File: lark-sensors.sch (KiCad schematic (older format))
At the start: 10 parts, among them IC1 MS5611-01BA03, IC2 MS5611-01BA03, U8 BMX055, U9 MS5525DSO

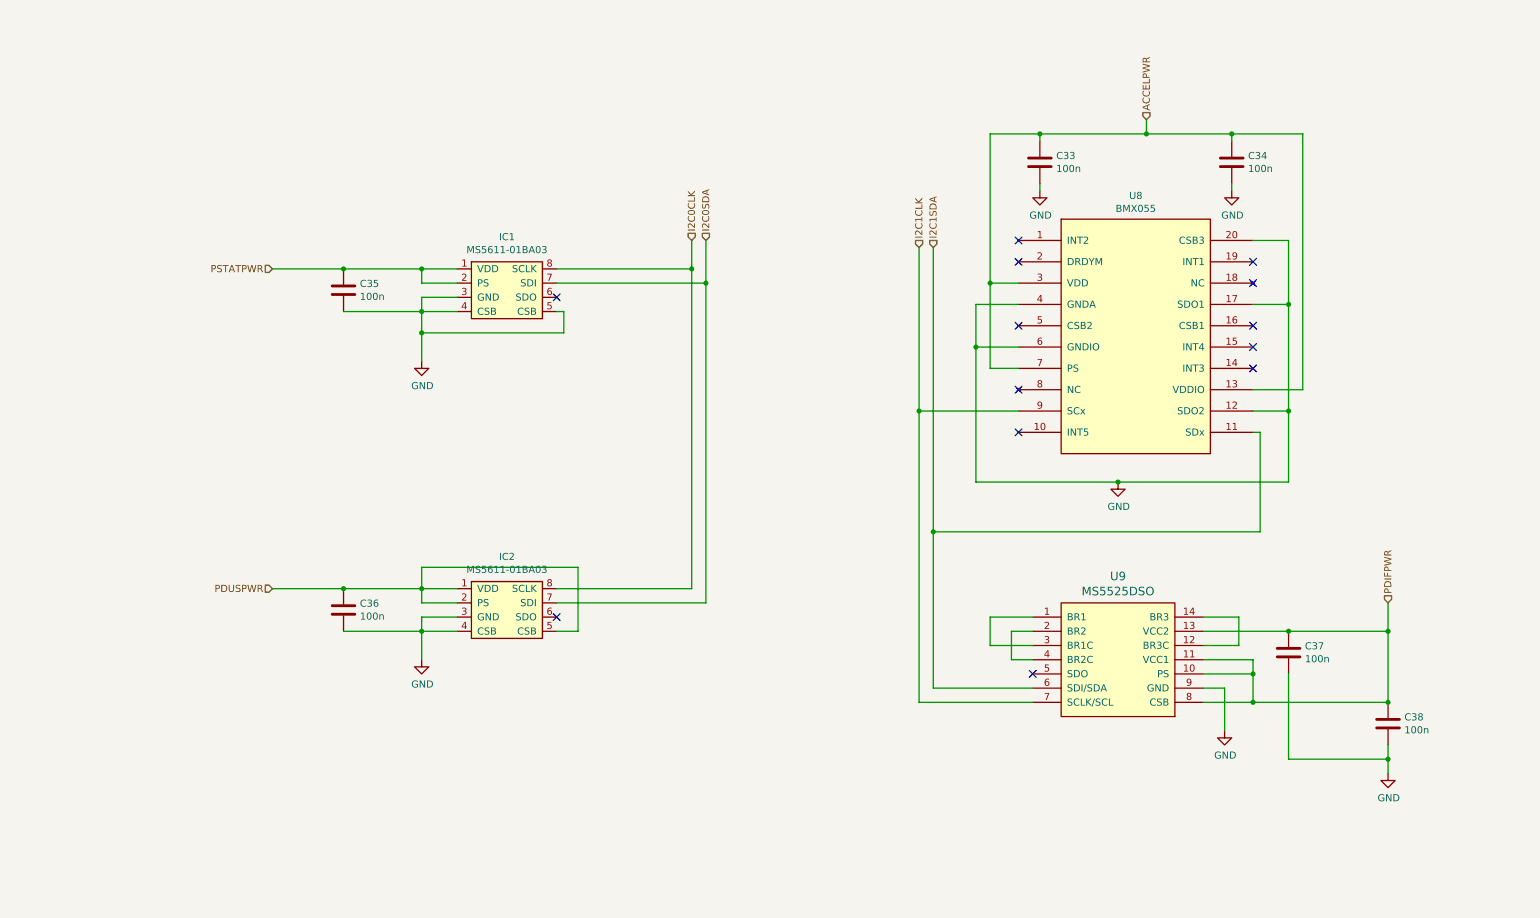
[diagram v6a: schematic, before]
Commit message: Updating schematic for the first prototype
* U1 can supply up to 600 mA
* drop USB charger for now
* smaller type of DC/DC (U2) for input
* remove one of the large capacitors
* change BMX interface to 4-wire SPI for speed reasons
* add I2C mux for pressure sensors

The changes were made during the meeting with Tomas.

BMX055 will be replaced by BMX088. For mechanical reasons, the pressure
sensors will be placed on a daughterboard. The daughterboard could get
footprints for different kinds pressure sensors (i.e. BMP388, HCLA0025).
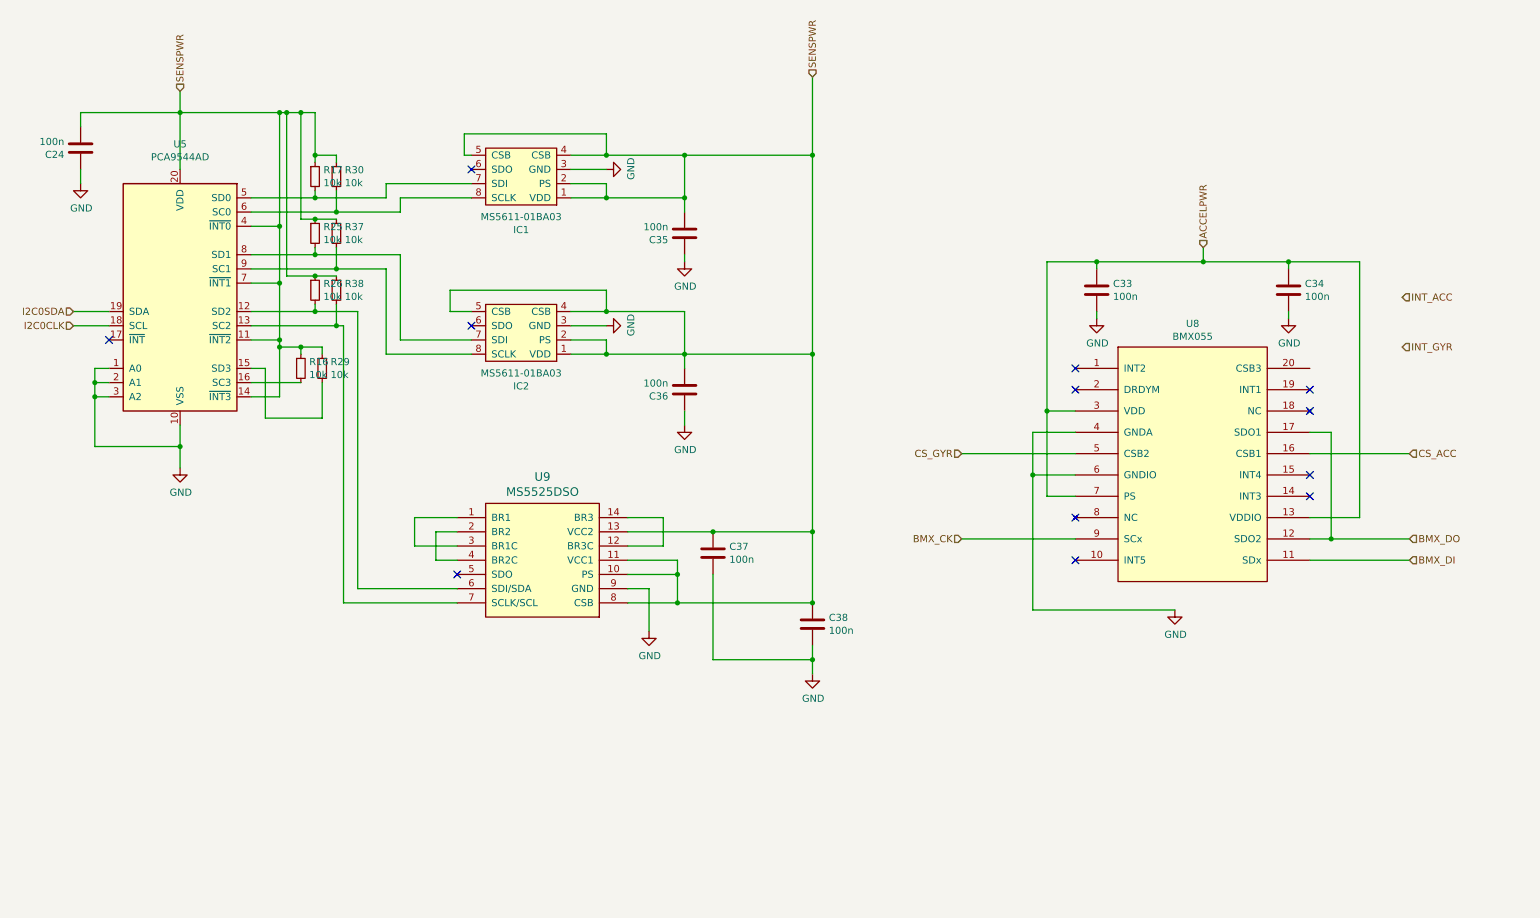
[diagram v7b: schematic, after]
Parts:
- added C24: 100n, Capacitor_SMD:C_0805_2012Metric_Pad1.15x1.40mm_HandSolder, symbol lark-rescue:C-Device
- added R16, R17, R25, R26, R29, R30, R37, R38: 10k, Resistor_SMD:R_0805_2012Metric_Pad1.15x1.40mm_HandSolder, symbol Device:R_Small
- added U5: PCA9544AD, Package_SO:SOIC-20W_7.5x12.8mm_P1.27mm, symbol Interface_Expansion:PCA9544AD
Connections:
- net GND: now also C35.1, C36.1, C24.1, U5.1 (A0), U5.10 (VSS), U5.2 (A1), U5.3 (A2); no longer C35.2, C36.2, IC1.4 (CSB), IC1.5 (CSB), IC2.4 (CSB), U8.12 (SDO2), U8.17 (SDO1), U8.20 (CSB3)
- net I2C0CLK: now also U5.18 (SCL); no longer IC1.8 (SCLK), IC2.8 (SCLK)
- net I2C0SDA: now also U5.19 (SDA); no longer IC1.7 (SDI), IC2.7 (SDI)
- net CS_ACC: now reaches U8.16 (CSB1)
- net CS_GYR: now reaches U8.5 (CSB2)
- net I2C1CLK: no longer names the net of U9.7 (SCLK/SCL)
- net I2C1CLK: now also R38.2, U5.13 (SC2); no longer U8.9 (SCx)
- net I2C1SDA: no longer names the net of U9.6 (SDI/SDA)
- net I2C1SDA: now also R26.2, U5.12 (SD2); no longer U8.11 (SDx)
- net PDIFPWR renamed SENSPWR
- net SENSPWR: now also C35.2, C36.2, IC1.1 (VDD), IC1.2 (PS), IC1.4 (CSB), IC1.5 (CSB), IC2.1 (VDD), IC2.2 (PS), IC2.4 (CSB), IC2.5 (CSB), C24.2, R16.1, R17.1, R25.1, R26.1, R29.1, R30.1, R37.1, R38.1, U5.11 (~INT2), U5.14 (~INT3), U5.20 (VDD), U5.4 (~INT0), U5.7 (~INT1)
- removed net PDUSPWR: C36.1, IC2.1 (VDD), IC2.2 (PS), IC2.5 (CSB)
- removed net PSTATPWR: C35.1, IC1.1 (VDD), IC1.2 (PS)
- new net: IC1.7 (SDI), R17.2, U5.5 (SD0)
- new net: IC1.8 (SCLK), R30.2, U5.6 (SC0)
- new net: IC2.7 (SDI), R25.2, U5.8 (SD1)
- new net: IC2.8 (SCLK), R37.2, U5.9 (SC1)
- new net: R29.2, U5.15 (SD3)
- new net: R16.2, U5.16 (SC3)
- new net BMX_CK: U8.9 (SCx)
- new net BMX_DI: U8.11 (SDx)
- new net BMX_DO: U8.12 (SDO2), U8.17 (SDO1)
- no-connect marks 13 -> 12
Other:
- moved on the sheet: C33, C34, C35, C36, C37, C38, IC1, IC2, U8, U9

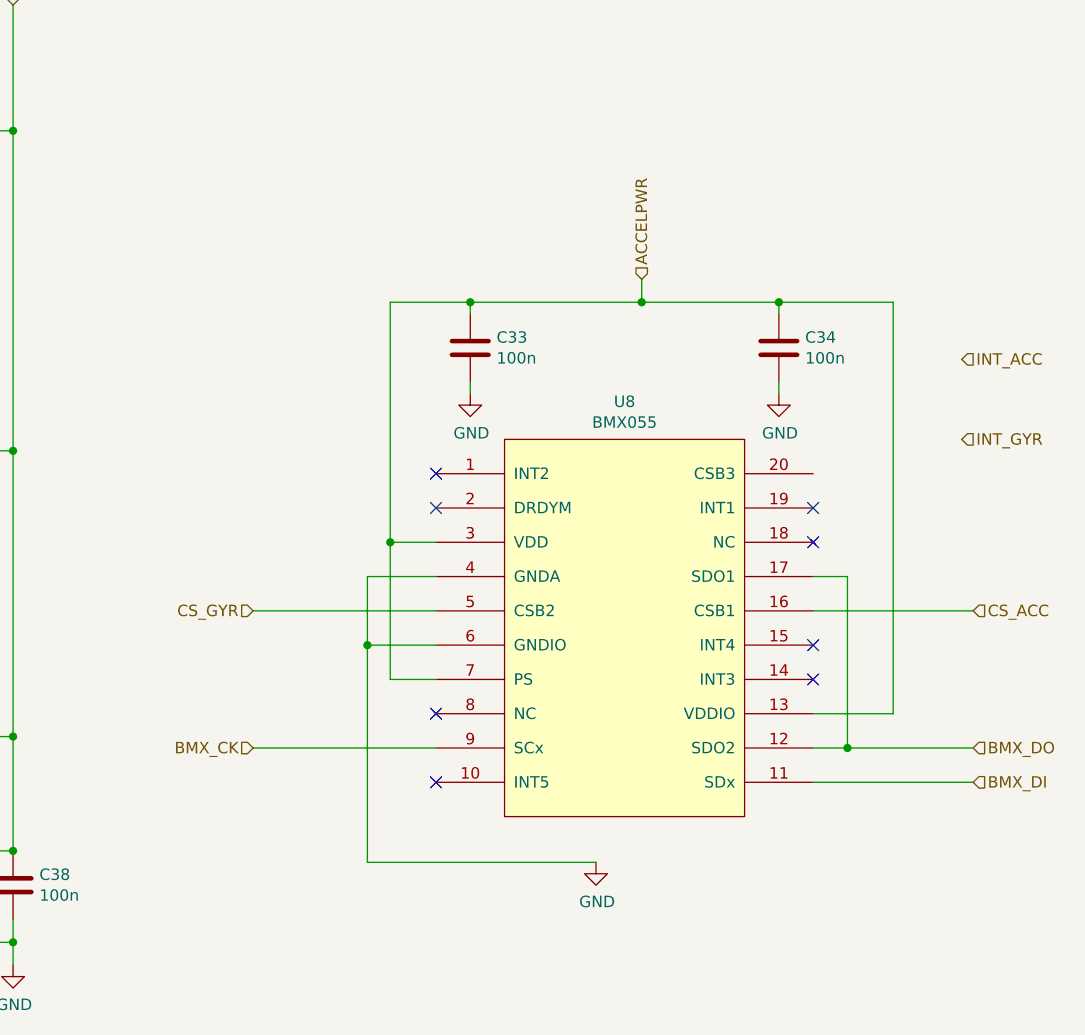
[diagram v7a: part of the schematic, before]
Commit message: Use BMI088 instead of BMX055.
Symbol for BMI088 was created and placed in the schematic.

Still looking for a LGA-16 4.5x3.0 footprint. Do we really need to
create that ourselves?
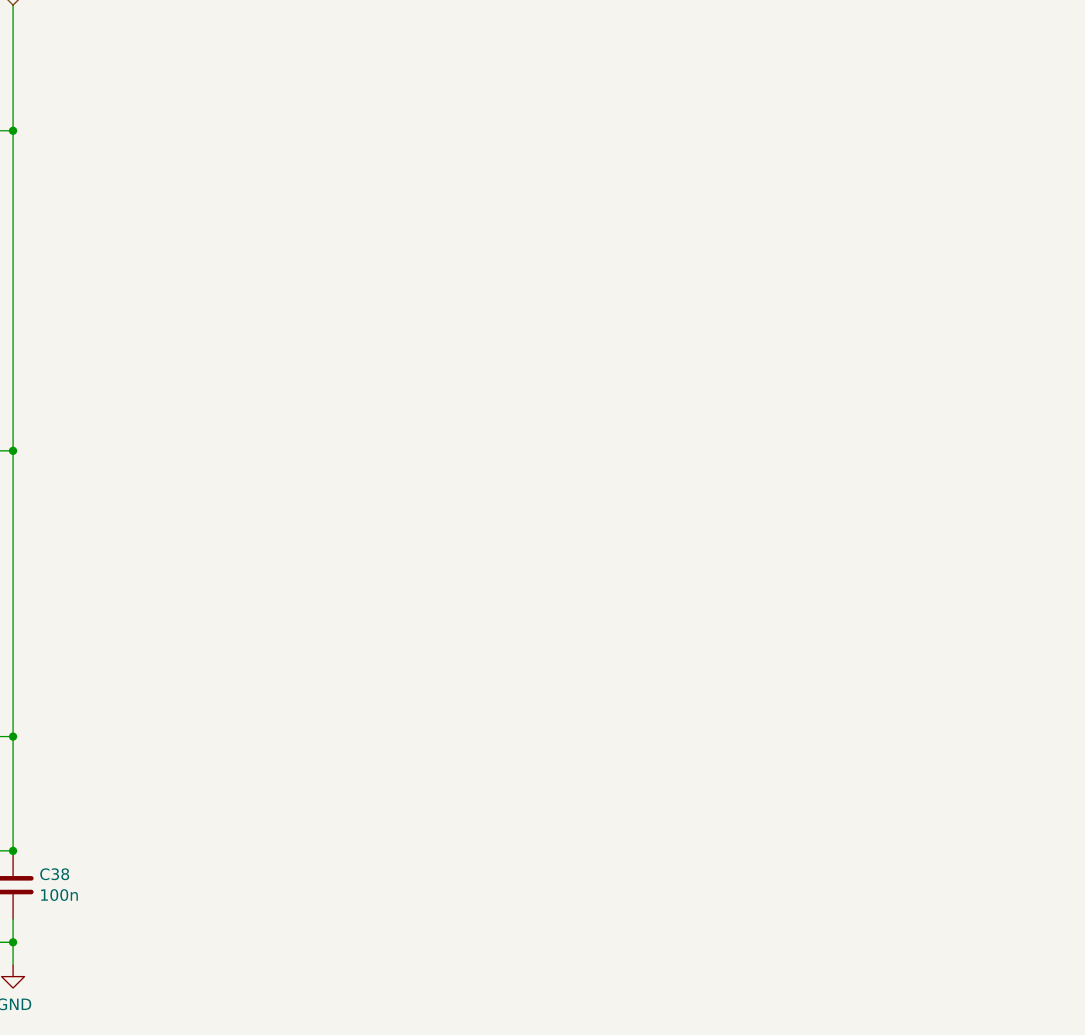
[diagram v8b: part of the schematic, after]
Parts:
- removed C33, C34: 100n, Capacitor_SMD:C_0805_2012Metric_Pad1.15x1.40mm_HandSolder, symbol lark-rescue:C-Device
- removed U8: BMX055, BMX055:BMX055, symbol lark-rescue:BMX055-bmx055
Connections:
- no-connect marks 12 -> 4
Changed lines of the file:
@@
 Text HLabel 1050 2650 0    50   Input ~ 0
 I2C0SDA
-$Comp
-L lark-rescue:GND-power #PWR038
-U 1 1 5C58F414
-P 8800 4750
-F 0 "#PWR038" H 8800 4500 50  0001 C CNN
-F 1 "GND" H 8805 4577 50  0000 C CNN
-F 2 "" H 8800 4750 50  0001 C CNN
-F 3 "" H 8800 4750 50  0001 C CNN
-	1    8800 4750
-	1    0    0    -1
-$EndComp
-$Comp
-L lark-rescue:C-Device C34
-U 1 1 5C593811
-P 9600 2500
-F 0 "C34" H 9715 2546 50  0000 L CNN
-F 1 "100n" H 9715 2455 50  0000 L CNN
-F 2 "Capacitor_SMD:C_0805_2012Metric_Pad1.15x1.40mm_HandSolder" H 9638 2350 50  0001 C CNN
-F 3 "~" H 9600 2500 50  0001 C CNN
-F 4 "885012207128" H 9600 2500 50  0001 C CNN "MPN"
-	1    9600 2500
-	1    0    0    -1
-$EndComp
-$Comp
-L lark-rescue:C-Device C33
-U 1 1 5C593886
-P 8250 2500
-F 0 "C33" H 8365 2546 50  0000 L CNN
-F 1 "100n" H 8365 2455 50  0000 L CNN
-F 2 "Capacitor_SMD:C_0805_2012Metric_Pad1.15x1.40mm_HandSolder" H 8288 2350 50  0001 C CNN
-F 3 "~" H 8250 2500 50  0001 C CNN
-F 4 "885012207128" H 8250 2500 50  0001 C CNN "MPN"
-	1    8250 2500
-	1    0    0    -1
-$EndComp
-Text HLabel 9000 2200 1    50   Input ~ 0
-ACCELPWR
-$Comp
-L lark-rescue:GND-power #PWR036
-U 1 1 5C59D0F5
-P 9600 2700
-F 0 "#PWR036" H 9600 2450 50  0001 C CNN
-F 1 "GND" H 9605 2527 50  0000 C CNN
-F 2 "" H 9600 2700 50  0001 C CNN
-F 3 "" H 9600 2700 50  0001 C CNN
-	1    9600 2700
-	1    0    0    -1
-$EndComp
-$Comp
-L lark-rescue:GND-power #PWR035
-U 1 1 5C59D1AD
-P 8250 2700
-F 0 "#PWR035" H 8250 2450 50  0001 C CNN
-F 1 "GND" H 8255 2527 50  0000 C CNN
-F 2 "" H 8250 2700 50  0001 C CNN
-F 3 "" H 8250 2700 50  0001 C CNN
-	1    8250 2700
-	1    0    0    -1
-$EndComp
 Wire Wire Line
 	5550 4200 6250 4200
@@
 	4800 1850 5350 1850
 NoConn ~ 3850 1650
-NoConn ~ 9750 3350
-NoConn ~ 9750 3200
-NoConn ~ 8100 4100
-NoConn ~ 8100 4400
-Wire Wire Line
-	9750 4100 10100 4100
-Wire Wire Line
-	10100 4100 10100 2300
-Wire Wire Line
-	8100 3350 7900 3350
-Wire Wire Line
-	7900 3350 7900 2300
-NoConn ~ 9750 3800
-NoConn ~ 9750 3950
-NoConn ~ 8100 3050
-NoConn ~ 8100 3200
-Wire Wire Line
-	7900 3350 7900 3950
-Wire Wire Line
-	7900 3950 8100 3950
-Connection ~ 7900 3350
-Wire Wire Line
-	8100 3500 7800 3500
-Wire Wire Line
-	7800 4750 8800 4750
-Wire Wire Line
-	8100 3800 7800 3800
-Wire Wire Line
-	7900 2300 8250 2300
-Wire Wire Line
-	8250 2350 8250 2300
-Connection ~ 8250 2300
-Wire Wire Line
-	8250 2700 8250 2650
-Wire Wire Line
-	9600 2350 9600 2300
-Connection ~ 9600 2300
-Wire Wire Line
-	9600 2300 10100 2300
-Wire Wire Line
-	9600 2650 9600 2700
-Wire Wire Line
-	8250 2300 9000 2300
-Wire Wire Line
-	9000 2200 9000 2300
-Connection ~ 9000 2300
-Wire Wire Line
-	9000 2300 9600 2300
 Wire Wire Line
 	3850 1850 3350 1850
@@
 	2500 2900 2500 2850
 Wire Wire Line
-	7800 3500 7800 3800
-Connection ~ 7800 3800
-Wire Wire Line
-	7800 3800 7800 4750
-Wire Wire Line
 	1050 2750 1300 2750
 Wire Wire Line
 	1300 2650 1050 2650
 NoConn ~ 1300 2850
-$Comp
-L lark-rescue:BMX055-bmx055 U8
-U 1 1 5C6812A2
-P 8900 3700
-AR Path="/5C6812A2" Ref="U8"  Part="1"
-AR Path="/5C4F6DA1/5C6812A2" Ref="U8"  Part="1"
-F 0 "U8" H 8925 4665 50  0000 C CNN
-F 1 "BMX055" H 8925 4574 50  0000 C CNN
-F 2 "BMX055:BMX055" H 9000 3700 50  0001 C CNN
-F 3 "" H 9000 3700 50  0001 C CNN
-F 4 "828-1060-1-ND " H 8900 3700 50  0001 C CNN "MPN"
-	1    8900 3700
-	1    0    0    -1
-$EndComp
-Wire Wire Line
-	8100 3650 7300 3650
-Wire Wire Line
-	9750 3650 10450 3650
-Wire Wire Line
-	9750 3500 9900 3500
-Wire Wire Line
-	9750 4400 10450 4400
-Wire Wire Line
-	9900 4250 9900 3500
-Wire Wire Line
-	9750 4250 9900 4250
-Wire Wire Line
-	9900 4250 10450 4250
-Connection ~ 9900 4250
-Text HLabel 10450 3650 2    50   Input ~ 0
-CS_ACC
-Text HLabel 7300 3650 0    50   Input ~ 0
-CS_GYR
-Text HLabel 10450 4250 2    50   Input ~ 0
-BMX_DO
-Text HLabel 10450 4400 2    50   Input ~ 0
-BMX_DI
-Wire Wire Line
-	8100 4250 7300 4250
-Text HLabel 7300 4250 0    50   Input ~ 0
-BMX_CK
-Text HLabel 10400 2550 2    50   Input ~ 0
-INT_ACC
-Text HLabel 10400 2900 2    50   Input ~ 0
-INT_GYR
 $EndSCHEMATC
